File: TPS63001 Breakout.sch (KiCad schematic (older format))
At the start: 15 parts, among them P1 CONN_01X01, P2 CONN_01X01, P3 CONN_01X05, U1 TPS63001

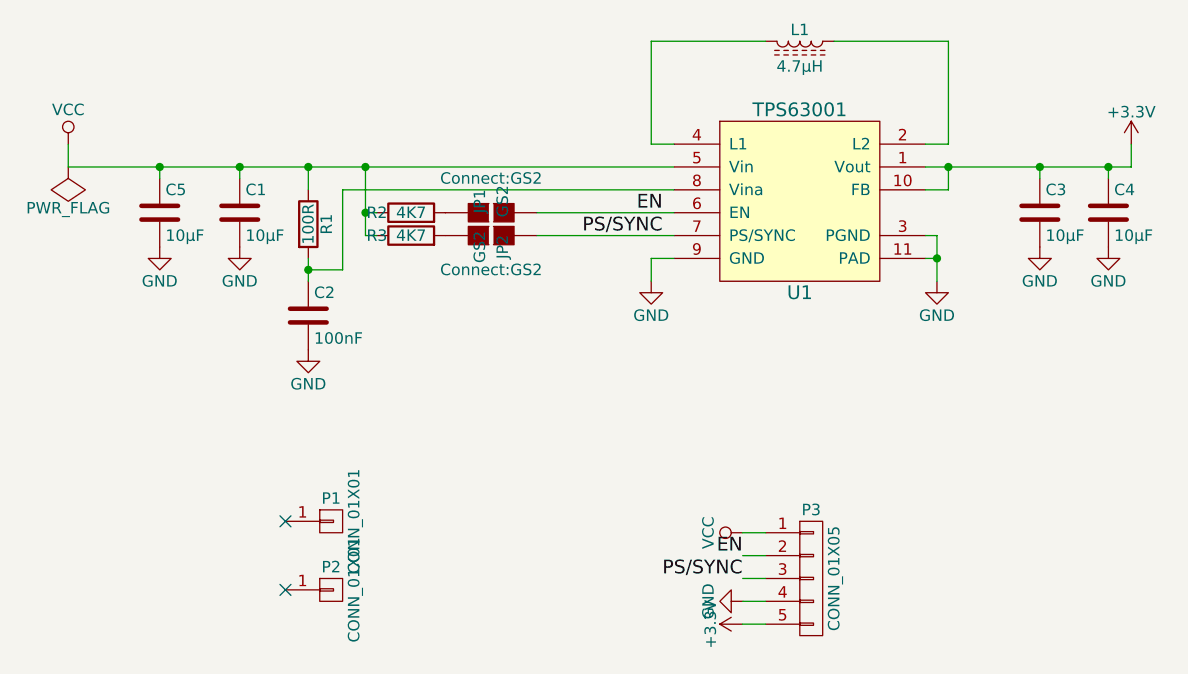
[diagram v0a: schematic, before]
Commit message: change pullups for PS/SYNC and EN to VCCA filtered supply
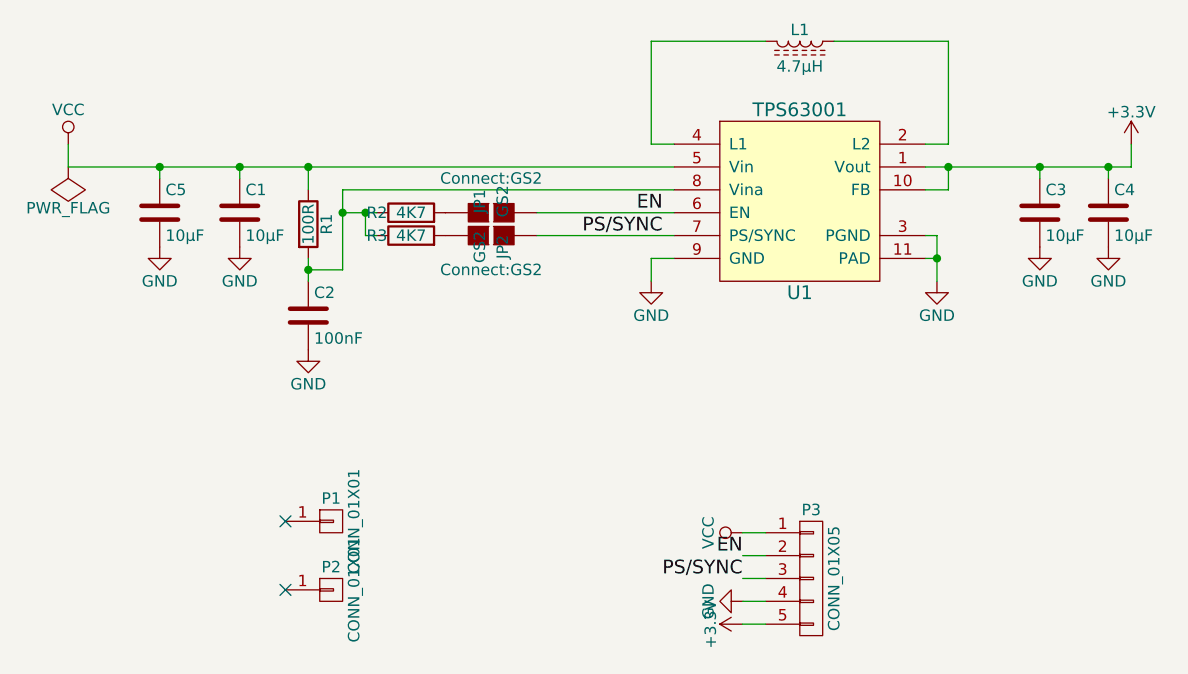
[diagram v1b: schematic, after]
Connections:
- net VCC: no longer R2.1, R3.1
- net at C2.1, R1.2, U1.8 (Vina): now also R2.1, R3.1
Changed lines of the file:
@@
 	3850 3250 3900 3250
 Wire Wire Line
-	3850 2950 3850 3250
-Connection ~ 3850 2950
-Wire Wire Line
-	3900 3150 3850 3150
+	3750 3150 3900 3150
 Connection ~ 3850 3150
 $Comp
@@
 	1    0    0    -1
 $EndComp
+Wire Wire Line
+	3850 3150 3850 3250
+Connection ~ 3750 3150
 $EndSCHEMATC
